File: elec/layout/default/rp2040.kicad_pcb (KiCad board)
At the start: 2 copper layers, 20 parts

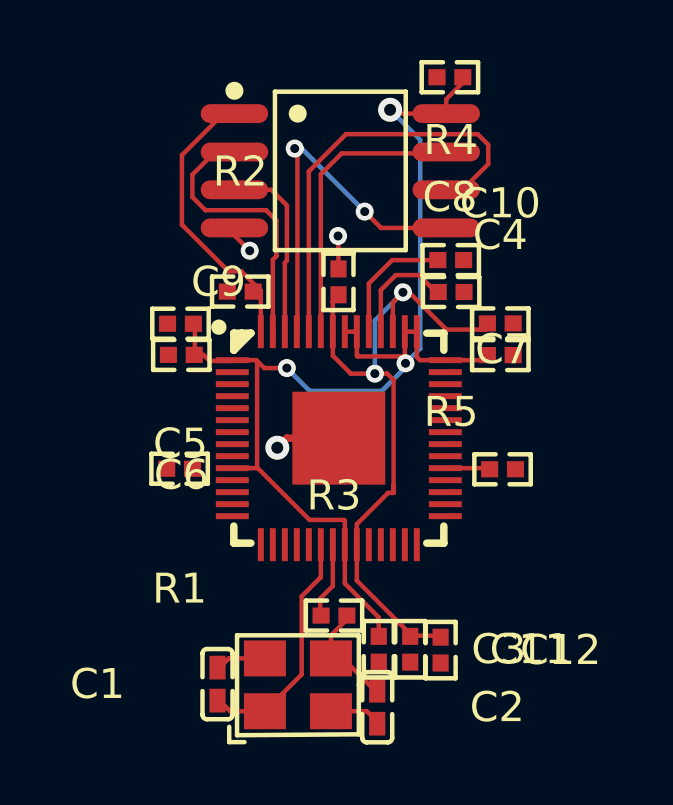
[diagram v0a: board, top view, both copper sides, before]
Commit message: update to kicad 9
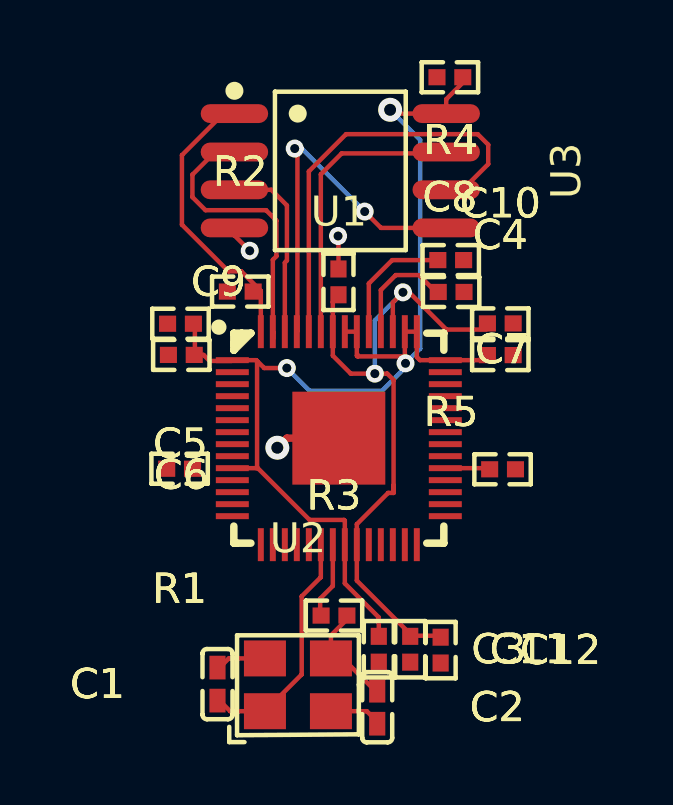
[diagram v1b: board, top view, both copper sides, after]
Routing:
- net cs-1: track 9.55 -> 0.00 mm
- net cs: track 0.00 -> 9.55 mm
- net out: track 3.72 -> 0.00 mm
- net osc-out: track 0.00 -> 3.72 mm

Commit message: build with latest
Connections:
- net scl renamed gpio21
- net sda renamed gpio20
- R2 pad 2: cs -> cs-1
- U1 pad 12: cs-1 -> cs
- U1 pad 13: sck -> sck-1
- U1 pad 52: sck-1 -> sck
- U1 pad 56: cs -> cs-1
- U3 pad 1: cs -> cs-1
- U3 pad 6: sck-1 -> sck
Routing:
- net sck-1: track 14.4 -> 0.00 mm
- net sck: track 0.00 -> 14.4 mm
- net cs-1: track 0.00 -> 9.55 mm
- net cs: track 9.55 -> 0.00 mm
